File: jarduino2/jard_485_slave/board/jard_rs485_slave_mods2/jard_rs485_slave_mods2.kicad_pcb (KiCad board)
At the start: 2 copper layers, 79.2 x 30 mm, 43 parts, among them J1 POWER, J3 Débit, J4 Niveaux, J6 EV1, Q4 BPC_FMMT38C, Q6 P03P4L-04, U1 BPC_Mod485, U6 BPC_DHT22

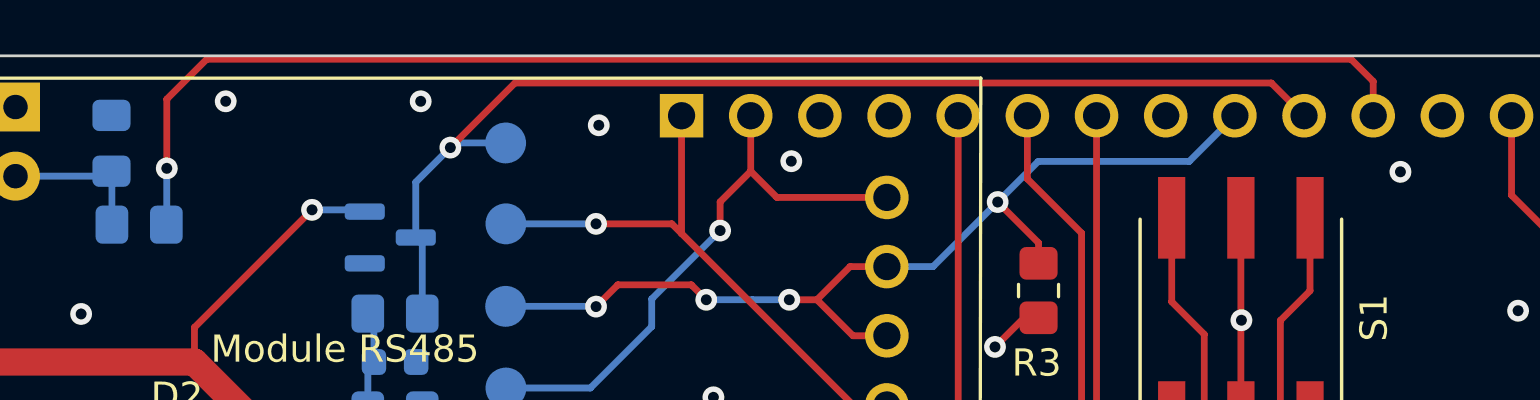
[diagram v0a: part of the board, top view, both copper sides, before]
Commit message: Déplacement piste LED car trop proche du bord
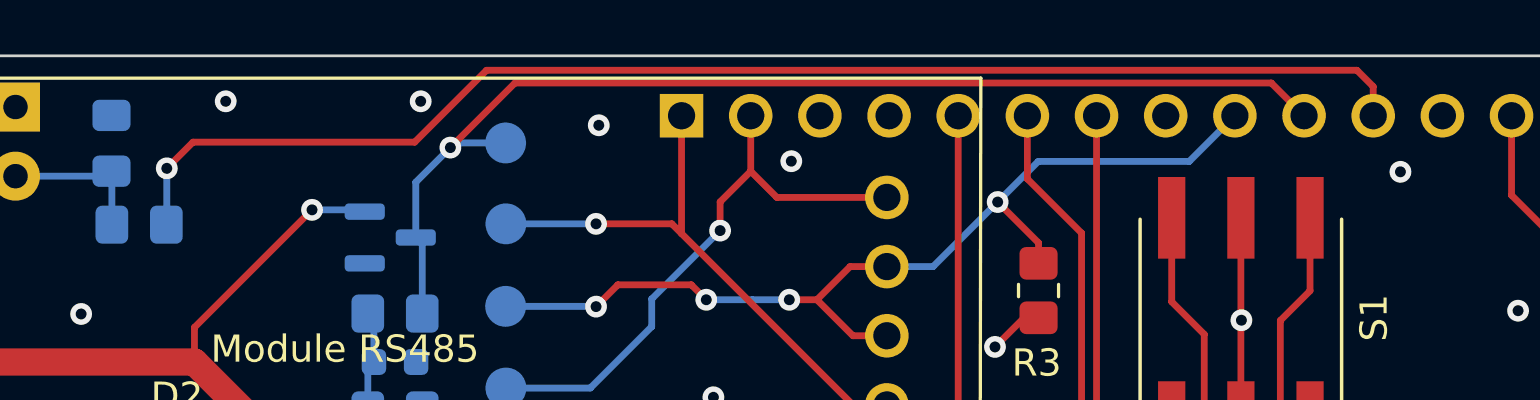
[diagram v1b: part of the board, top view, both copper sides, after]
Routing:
- net LED: track 51.1 -> 49.2 mm
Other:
- board text added: "27/04/2024"
- board text added: "Esclave OYA Rev F0 BPC 2024"
- board text removed: "13/04/2024"
- board text removed: "Esclave OYA Rev E0 BPC 2024"
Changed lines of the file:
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@@
   (title_block
     (title "Carte de commande d'un OYA - Esclave RS485")
-    (date "2024-04-13")
-    (rev "E0")
+    (date "2024-04-27")
+    (rev "F0")
     (company "BPC")
     (comment 1 "Technologie avec modules Arduino / Petite carte")
@@
     (effects (font (size 0.8 0.8) (thickness 0.1)) (justify left bottom mirror))
   )
-  (gr_text "13/04/2024" (at 114.39 114.28 270) (layer "B.SilkS")
+  (gr_text "27/04/2024" (at 114.39 114.28 270) (layer "B.SilkS")
     (effects (font (size 0.8 0.8) (thickness 0.1)) (justify left bottom mirror))
   )
-  (gr_text "Esclave OYA\nRev E0\nBPC 2024" (at 125.984 112.522 -90) (layer "B.SilkS")
+  (gr_text "Esclave OYA\nRev F0\nBPC 2024" (at 125.984 112.522 270) (layer "B.SilkS")
     (effects (font (size 1 1) (thickness 0.15)) (justify left bottom mirror))
   )
@@
   (segment (start 158.09 107.34) (end 159.2 107.34) (width 0.25) (layer "B.Cu") (net 20))
   (segment (start 157.54 110) (end 157.54 107.89) (width 0.25) (layer "B.Cu") (net 20))
-  (segment (start 174.86 87.738) (end 174.047 86.925) (width 0.25) (layer "F.Cu") (net 21))
-  (segment (start 174.047 86.925) (end 132.023 86.925) (width 0.25) (layer "F.Cu") (net 21))
-  (segment (start 132.023 86.925) (end 130.556 88.392) (width 0.25) (layer "F.Cu") (net 21))
-  (segment (start 174.86 89) (end 174.86 87.738) (width 0.25) (layer "F.Cu") (net 21))
-  (segment (start 130.556 88.392) (end 130.556 90.932) (width 0.25) (layer "F.Cu") (net 21))
+  (segment (start 174.86 89) (end 174.86 87.93) (width 0.25) (layer "F.Cu") (net 21))
+  (segment (start 174.26 87.33) (end 142.3 87.33) (width 0.25) (layer "F.Cu") (net 21))
+  (segment (start 139.66 89.97) (end 131.518 89.97) (width 0.25) (layer "F.Cu") (net 21))
+  (segment (start 131.518 89.97) (end 130.556 90.932) (width 0.25) (layer "F.Cu") (net 21))
+  (segment (start 142.3 87.33) (end 139.66 89.97) (width 0.25) (layer "F.Cu") (net 21))
+  (segment (start 174.86 87.93) (end 174.26 87.33) (width 0.25) (layer "F.Cu") (net 21))
   (via (at 130.556 90.932) (size 0.8) (drill 0.4) (layers "F.Cu" "B.Cu") (net 21))
   (segment (start 130.556 92.984) (end 130.54 93) (width 0.25) (layer "B.Cu") (net 21))

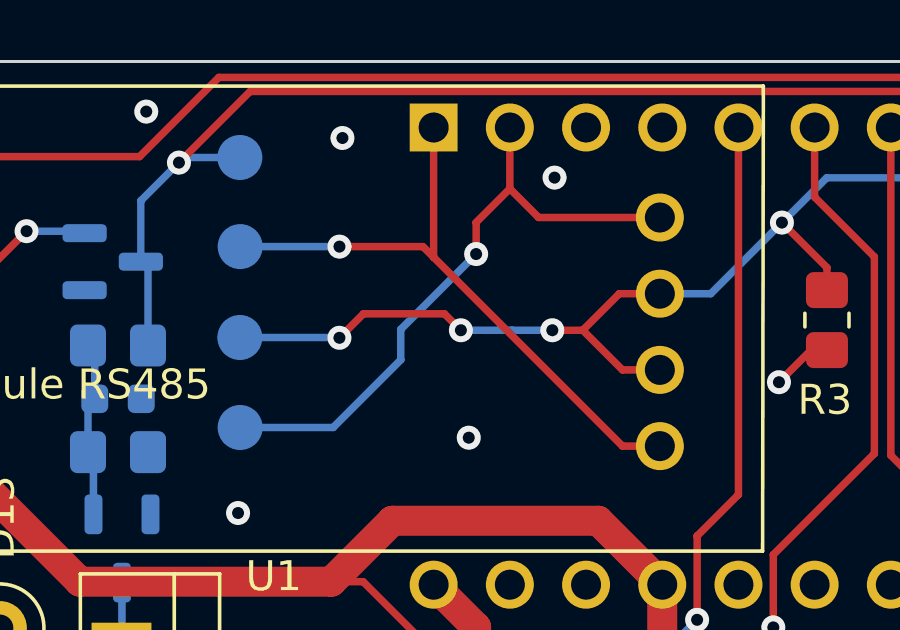
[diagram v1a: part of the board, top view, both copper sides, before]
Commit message: Inversion RX/TX 485
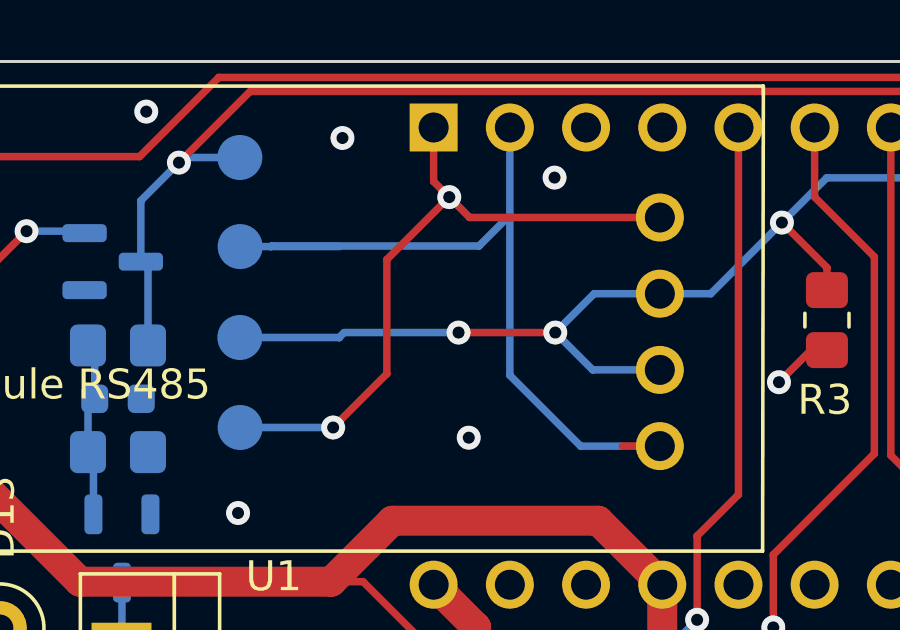
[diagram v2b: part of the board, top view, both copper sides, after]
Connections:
- TP1 pad 1: RX -> TX
- TP3 pad 1: TX -> RX
- U1 pad 5: RX -> TX
- U1 pad 8: TX -> RX
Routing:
- net RX: track 20.9 -> 27.2 mm, vias 1 -> 0
- net TX: track 21.1 -> 22.2 mm, vias 1 -> 2
- net TX_EN: track 36.1 -> 36.8 mm, vias 4 -> 3
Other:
- board text added: "04/05/2024"
- board text removed: "27/04/2024"
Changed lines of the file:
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@@
   (title_block
     (title "Carte de commande d'un OYA - Esclave RS485")
-    (date "2024-04-27")
+    (date "2024-05-04")
     (rev "F0")
     (company "BPC")
@@
     (descr "Terminal Block Phoenix MKDS-1,5-2-5.08, 2 pins, pitch 5.08mm, size 10.2x9.8mm^2, drill diamater 1.3mm, pad diameter 2.6mm, see http://www.farnell.com/datasheets/100425.pdf, script-generated using https://github.com/pointhi/kicad-footprint-generator/scripts/TerminalBlock_Phoenix")
     (tags "THT Terminal Block Phoenix MKDS-1,5-2-5.08 pitch 5.08mm size 10.2x9.8mm^2 drill 1.3mm pad 2.6mm")
+    (property "Description" "Bornier 2 contacts 5.08mm")
+    (property "Fabricant" "PHOENIX CONTACT")
+    (property "Fournisseur" "Farnell")
     (property "Sheetfile" "uc.kicad_sch")
     (property "Sheetname" "UC")
@@
     (at 116 99.62 90)
     (tags "Arduino RS485")
-    (property "Bpcref" "1")
+    (property "Bpcref" "")
+    (property "Description" "Module RS485 pour Arduino")
     (property "Sheetfile" "ES.kicad_sch")
     (property "Sheetname" "ES")
@@
       (net 2 "GND") (pinfunction "Gnd") (pintype "power_in"))
     (pad "5" thru_hole oval (at 7.62 41 90) (size 1.6 1.6) (drill 1) (layers "*.Cu" "*.Mask")
-      (net 5 "RX") (pinfunction "DI") (pintype "input"))
+      (net 9 "TX") (pinfunction "DI") (pintype "input"))
     (pad "6" thru_hole oval (at 5.08 41 90) (size 1.6 1.6) (drill 1) (layers "*.Cu" "*.Mask")
       (net 8 "TX_EN") (pinfunction "DE") (pintype "input"))
@@
       (net 8 "TX_EN") (pinfunction "RE") (pintype "input"))
     (pad "8" thru_hole oval (at 0 41 90) (size 1.6 1.6) (drill 1) (layers "*.Cu" "*.Mask")
-      (net 9 "TX") (pinfunction "RO") (pintype "output"))
+      (net 5 "RX") (pinfunction "RO") (pintype "output"))
     (model "${BPCLIBS}/bpc/3d/rs485.stp"
       (offset (xyz -3.3 1.5 3.5))
@@
       (stroke (width 0.05) (type solid)) (fill none) (layer "B.CrtYd"))
     (pad "1" smd circle (at 0 0 90) (size 1.5 1.5) (layers "B.Cu" "B.Mask")
-      (net 5 "RX") (pinfunction "1") (pintype "passive"))
+      (net 9 "TX") (pinfunction "1") (pintype "passive"))
   )
   (footprint "Resistor_SMD:R_0805_2012Metric_Pad1.20x1.40mm_HandSolder" (layer "B.Cu")
@@
       (stroke (width 0.05) (type solid)) (fill none) (layer "B.CrtYd"))
     (pad "1" smd circle (at 0 0 180) (size 1.5 1.5) (layers "B.Cu" "B.Mask")
-      (net 9 "TX") (pinfunction "1") (pintype "passive"))
+      (net 5 "RX") (pinfunction "1") (pintype "passive"))
   )
   (gr_line locked (start 192.585786 114.8) (end 192.585786 88.8)
@@
     (effects (font (size 0.8 0.8) (thickness 0.1)) (justify left bottom mirror))
   )
-  (gr_text "27/04/2024" (at 114.39 114.28 270) (layer "B.SilkS")
+  (gr_text "04/05/2024" (at 114.39 114.28 270) (layer "B.SilkS")
     (effects (font (size 0.8 0.8) (thickness 0.1)) (justify left bottom mirror))
   )
@@
   (segment (start 137.938 99.822) (end 137.938 98.269) (width 0.25) (layer "B.Cu") (net 4))
   (segment (start 137.938 98.269) (end 138.163 98.044) (width 0.25) (layer "B.Cu") (net 4))
-  (segment (start 152.96 92) (end 152 91.04) (width 0.25) (layer "F.Cu") (net 5))
-  (segment (start 157 92) (end 152.96 92) (width 0.25) (layer "F.Cu") (net 5))
-  (segment (start 152 91.04) (end 152 89) (width 0.25) (layer "F.Cu") (net 5))
-  (segment (start 150.876 92.164) (end 152 91.04) (width 0.25) (layer "F.Cu") (net 5))
-  (segment (start 150.876 93.218) (end 150.876 92.164) (width 0.25) (layer "F.Cu") (net 5))
-  (via (at 150.876 93.218) (size 0.8) (drill 0.4) (layers "F.Cu" "B.Cu") (net 5))
-  (segment (start 148.365 96.745) (end 146.11 99) (width 0.25) (layer "B.Cu") (net 5))
-  (segment (start 146.11 99) (end 143.01 99) (width 0.25) (layer "B.Cu") (net 5))
-  (segment (start 148.365 95.729) (end 148.365 96.745) (width 0.25) (layer "B.Cu") (net 5))
-  (segment (start 150.876 93.218) (end 148.365 95.729) (width 0.25) (layer "B.Cu") (net 5))
+  (segment (start 157 99.62) (end 155.754 99.62) (width 0.25) (layer "F.Cu") (net 5))
+  (segment (start 152 91.92) (end 152 89) (width 0.25) (layer "B.Cu") (net 5))
+  (segment (start 157 99.62) (end 154.36 99.62) (width 0.25) (layer "B.Cu") (net 5))
+  (segment (start 152 91.92) (end 150.97 92.95) (width 0.25) (layer "B.Cu") (net 5))
+  (segment (start 144.04 92.97) (end 146.32 92.97) (width 0.25) (layer "B.Cu") (net 5))
+  (segment (start 144.06 92.95) (end 144.04 92.97) (width 0.25) (layer "B.Cu") (net 5))
+  (segment (start 154.36 99.62) (end 152 97.26) (width 0.25) (layer "B.Cu") (net 5))
+  (segment (start 152 97.26) (end 152 91.92) (width 0.25) (layer "B.Cu") (net 5))
+  (segment (start 143.01 92.97) (end 144.04 92.97) (width 0.25) (layer "B.Cu") (net 5))
+  (segment (start 150.97 92.95) (end 144.06 92.95) (width 0.25) (layer "B.Cu") (net 5))
   (segment (start 190.65 101.2) (end 191.8 102.35) (width 0.25) (layer "F.Cu") (net 6))
   (segment (start 149.098 114.35) (end 150.318 115.57) (width 0.25) (layer "F.Cu") (net 6))
@@
   (segment (start 122.95 107.97) (end 123 107.92) (width 0.25) (layer "B.Cu") (net 7))
   (segment (start 119.64 107.97) (end 122.95 107.97) (width 0.25) (layer "B.Cu") (net 7))
-  (segment (start 154.432 95.758) (end 153.416 95.758) (width 0.25) (layer "F.Cu") (net 8))
-  (segment (start 154.432 95.758) (end 155.65 94.54) (width 0.25) (layer "F.Cu") (net 8))
   (segment (start 162.57 94.42) (end 162.57 93.67) (width 0.25) (layer "F.Cu") (net 8))
-  (segment (start 157 97.08) (end 155.754 97.08) (width 0.25) (layer "F.Cu") (net 8))
-  (segment (start 149.82 95.21) (end 150.368 95.758) (width 0.25) (layer "F.Cu") (net 8))
-  (segment (start 147.12 95.21) (end 149.82 95.21) (width 0.25) (layer "F.Cu") (net 8))
-  (segment (start 146.32 96.01) (end 147.12 95.21) (width 0.25) (layer "F.Cu") (net 8))
-  (segment (start 155.65 94.54) (end 157 94.54) (width 0.25) (layer "F.Cu") (net 8))
-  (segment (start 155.754 97.08) (end 154.432 95.758) (width 0.25) (layer "F.Cu") (net 8))
+  (segment (start 150.29 95.835) (end 153.515 95.835) (width 0.25) (layer "F.Cu") (net 8))
   (segment (start 162.57 93.67) (end 161.069 92.169) (width 0.25) (layer "F.Cu") (net 8))
-  (via (at 153.416 95.758) (size 0.8) (drill 0.4) (layers "F.Cu" "B.Cu") (net 8))
-  (via (at 146.32 96.01) (size 0.8) (drill 0.4) (layers "F.Cu" "B.Cu") (net 8))
+  (via (at 150.29 95.835) (size 0.8) (drill 0.4) (layers "F.Cu" "B.Cu") (net 8))
+  (via (at 153.515 95.835) (size 0.8) (drill 0.4) (layers "F.Cu" "B.Cu") (net 8))
   (via (at 161.069 92.169) (size 0.8) (drill 0.4) (layers "F.Cu" "B.Cu") (net 8))
-  (via (at 150.368 95.758) (size 0.8) (drill 0.4) (layers "F.Cu" "B.Cu") (net 8))
   (segment (start 158.698 94.54) (end 157 94.54) (width 0.25) (layer "B.Cu") (net 8))
+  (segment (start 153.34 96.01) (end 153.515 95.835) (width 0.25) (layer "B.Cu") (net 8))
   (segment (start 161.069 92.169) (end 158.698 94.54) (width 0.25) (layer "B.Cu") (net 8))
+  (segment (start 154.81 94.54) (end 157 94.54) (width 0.25) (layer "B.Cu") (net 8))
   (segment (start 143 96) (end 146.31 96) (width 0.25) (layer "B.Cu") (net 8))
-  (segment (start 153.416 95.758) (end 152.07 95.758) (width 0.25) (layer "B.Cu") (net 8))
-  (segment (start 152.07 95.758) (end 150.368 95.758) (width 0.25) (layer "B.Cu") (net 8))
+  (segment (start 150.29 95.835) (end 146.475 95.835) (width 0.25) (layer "B.Cu") (net 8))
+  (segment (start 153.515 95.835) (end 154.76 97.08) (width 0.25) (layer "B.Cu") (net 8))
+  (segment (start 154.76 97.08) (end 157 97.08) (width 0.25) (layer "B.Cu") (net 8))
   (segment (start 146.31 96) (end 146.32 96.01) (width 0.25) (layer "B.Cu") (net 8))
   (segment (start 168.102 90.678) (end 162.56 90.678) (width 0.25) (layer "B.Cu") (net 8))
   (segment (start 169.78 89) (end 168.102 90.678) (width 0.25) (layer "B.Cu") (net 8))
+  (segment (start 146.475 95.835) (end 146.31 96) (width 0.25) (layer "B.Cu") (net 8))
   (segment (start 162.56 90.678) (end 161.069 92.169) (width 0.25) (layer "B.Cu") (net 8))
-  (segment (start 146.32 92.97) (end 149.104 92.97) (width 0.25) (layer "F.Cu") (net 9))
-  (segment (start 157 99.62) (end 155.754 99.62) (width 0.25) (layer "F.Cu") (net 9))
-  (segment (start 155.754 99.62) (end 149.46 93.326) (width 0.25) (layer "F.Cu") (net 9))
-  (segment (start 149.104 92.97) (end 149.46 93.326) (width 0.25) (layer "F.Cu") (net 9))
-  (segment (start 149.46 93.326) (end 149.46 89) (width 0.25) (layer "F.Cu") (net 9))
-  (via (at 146.32 92.97) (size 0.8) (drill 0.4) (layers "F.Cu" "B.Cu") (net 9))
-  (segment (start 143.01 92.97) (end 146.32 92.97) (width 0.25) (layer "B.Cu") (net 9))
+  (segment (start 153.515 95.835) (end 154.81 94.54) (width 0.25) (layer "B.Cu") (net 8))
+  (segment (start 149.98 91.32) (end 147.9 93.4) (width 0.25) (layer "F.Cu") (net 9))
+  (segment (start 149.46 90.8) (end 149.46 89) (width 0.25) (layer "F.Cu") (net 9))
+  (segment (start 147.9 97.21) (end 146.11 99) (width 0.25) (layer "F.Cu") (net 9))
+  (segment (start 157 92) (end 150.66 92) (width 0.25) (layer "F.Cu") (net 9))
+  (segment (start 150.66 92) (end 149.98 91.32) (width 0.25) (layer "F.Cu") (net 9))
+  (segment (start 147.9 93.4) (end 147.9 97.21) (width 0.25) (layer "F.Cu") (net 9))
+  (segment (start 149.98 91.32) (end 149.46 90.8) (width 0.25) (layer "F.Cu") (net 9))
+  (via (at 146.11 99) (size 0.8) (drill 0.4) (layers "F.Cu" "B.Cu") (net 9))
+  (via (at 149.98 91.32) (size 0.8) (drill 0.4) (layers "F.Cu" "B.Cu") (net 9))
+  (segment (start 143.01 99) (end 146.11 99) (width 0.25) (layer "B.Cu") (net 9))
   (segment (start 185.21 101.53) (end 175.838 101.53) (width 0.25) (layer "F.Cu") (net 10))
   (segment (start 185.54 101.2) (end 185.21 101.53) (width 0.25) (layer "F.Cu") (net 10))
